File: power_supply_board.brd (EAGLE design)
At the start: 100 x 65 mm, 30 parts, among them J6 1744426-2

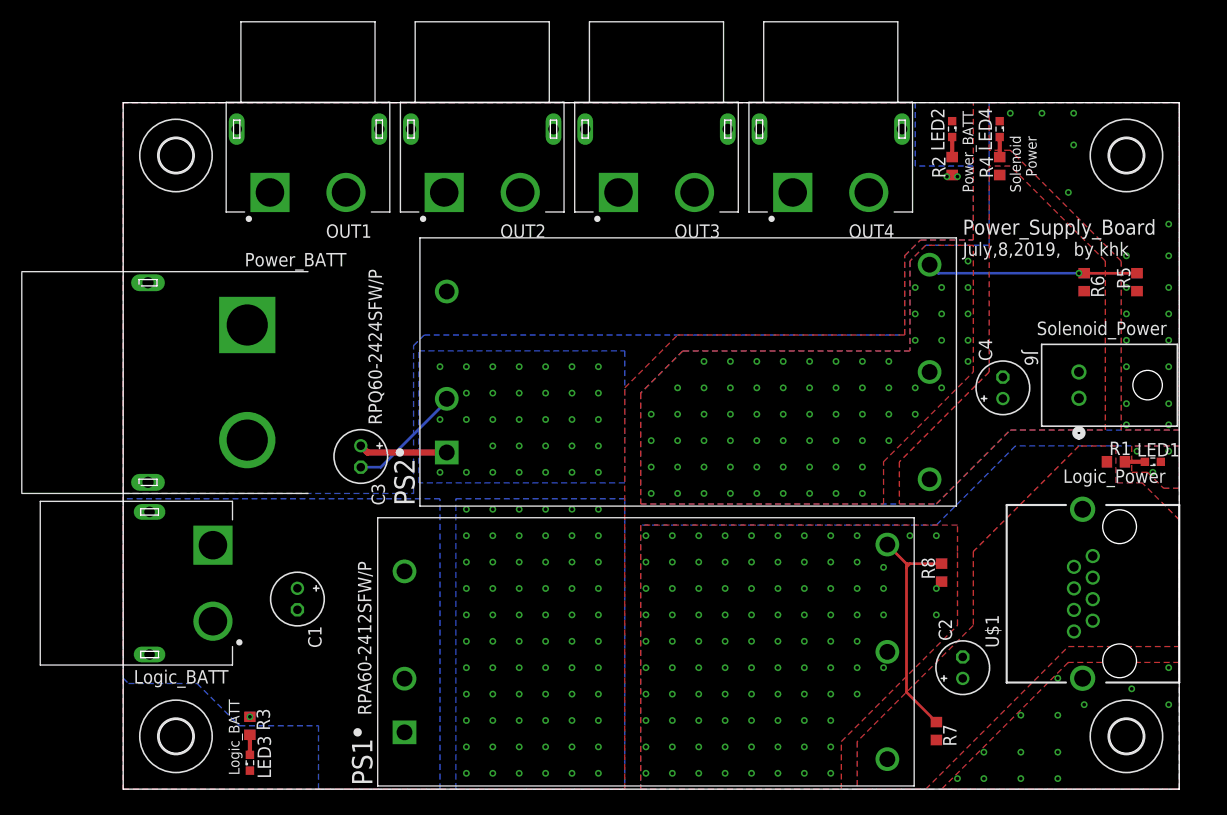
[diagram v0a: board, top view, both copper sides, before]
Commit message: 配線ミスを修正
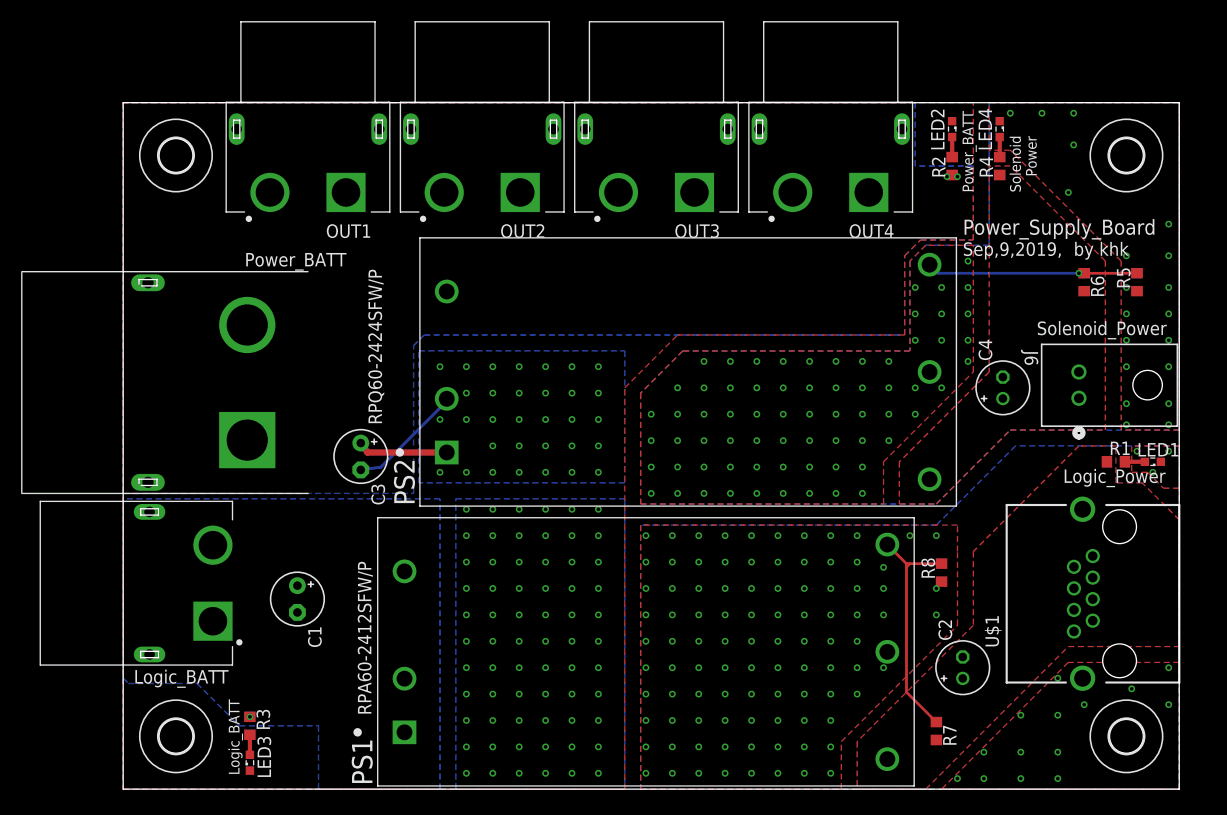
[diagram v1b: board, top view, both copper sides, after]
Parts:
- C1, C3: value (none) -> 220u; device rcl:E2-5 -> rcl:E2,5-5
- C2, C4: value (none) -> 100u
- LED3: value (none) -> green_3V_5mA
- OUT1, OUT2, OUT3, OUT4: value XT60PW-F -> XT60PW-M; device XT60_Connecotr:AMASS_XT60PW_F -> XT60_Connecotr:AMASS_XT60PW_M
- POWER1: value XT60PW-M -> XT60PW-F; device XT60_Connecotr:AMASS_XT60PW-M -> XT60_Connecotr:AMASS_XT60PW-F
- POWER2: value XT90PW_M -> XT90PW_F; device XT60_Connecotr:AMASS_XT90PW_M -> XT60_Connecotr:AMASS_XT90PW_F
- R1: value (none) -> 2k2
- R3, R4: value (none) -> 4k7
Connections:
- net DGND: now also OUT1.2, OUT2.2, OUT3.2, OUT4.2, POWER1.1, POWER2.1; no longer OUT1.1, OUT2.1, OUT3.1, OUT4.1, POWER1.2, POWER2.2, PS1.3, PS2.3
- net LOGIC_BATT: now also POWER1.2; no longer POWER1.1
- net POWER_BATT: now also OUT1.1, OUT2.1, OUT3.1, OUT4.1, POWER2.2; no longer OUT1.2, OUT2.2, OUT3.2, OUT4.2, POWER2.1
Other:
- board text added: "Sep,9,2019,"
- board text removed: "July,8,2019,"
